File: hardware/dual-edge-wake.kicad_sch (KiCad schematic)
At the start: 31 parts, among them J1 Conn_01x04_Male, J2 Circuit, J3 Falling, J4 Leading, J5 Output pull-up, J6 Output bias, J7 Vcc LED, J8 Input LED, J9 Output LED, Q1 BC807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

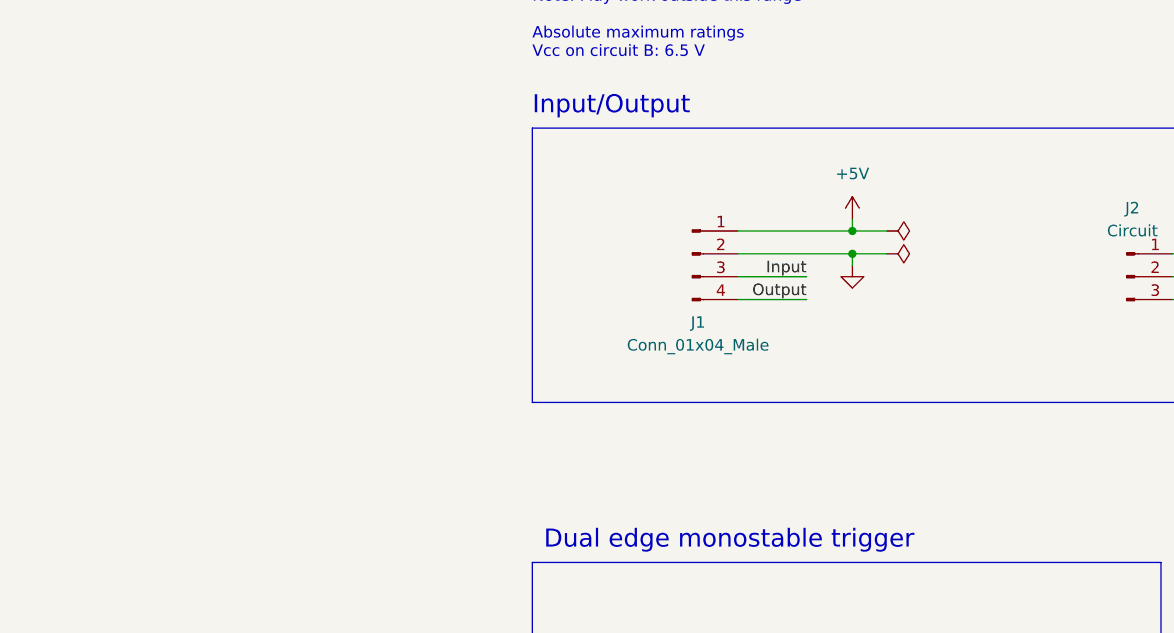
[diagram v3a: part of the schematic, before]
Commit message: Add input resistor
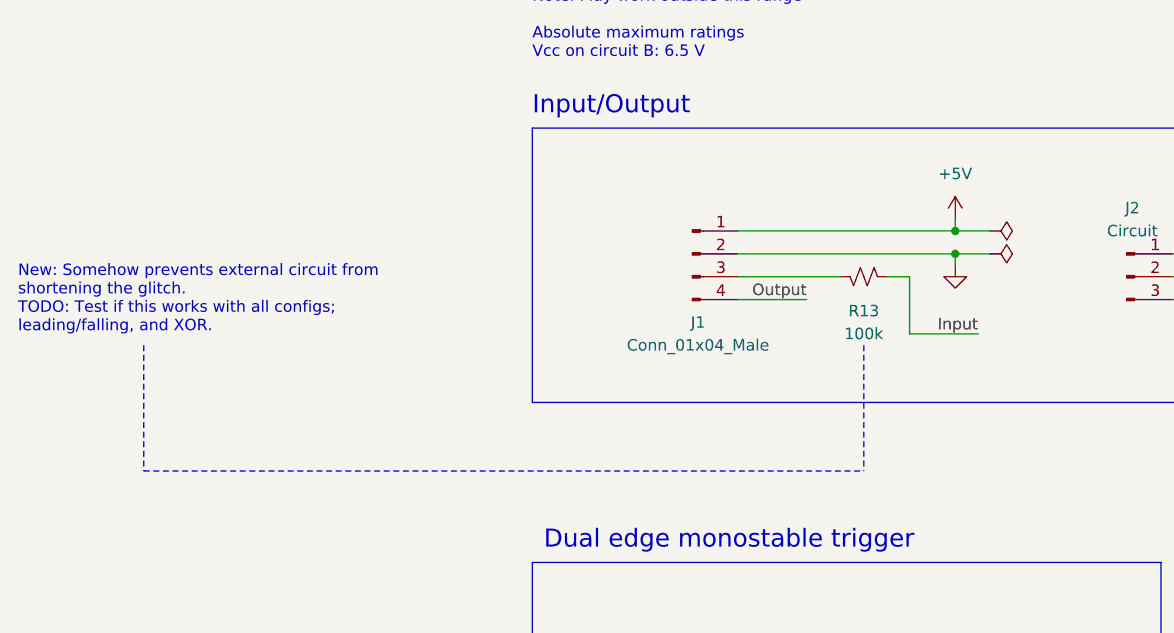
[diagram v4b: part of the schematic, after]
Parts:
- added R13: 100k, Resistor_SMD:R_0805_2012Metric_Pad1.20x1.40mm_HandSolder, symbol Device:R_Small_US
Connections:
- net Input: now also R13.1; no longer J1.3 (Pin_3)
- new net: J1.3 (Pin_3), R13.2
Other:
- note added: "New: Somehow prevents external circuit from shortening the glitch. TODO: Test if this works with all configs; leading/falling, and XOR."
